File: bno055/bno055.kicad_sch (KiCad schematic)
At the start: 0 parts

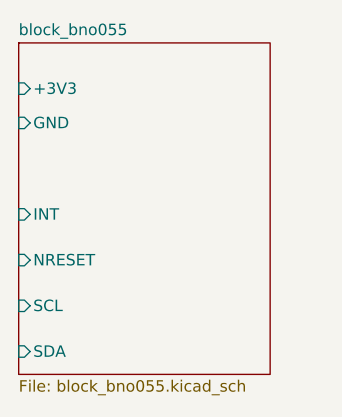
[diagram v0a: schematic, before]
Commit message: [Rushil] corrected pcb added information on both schematic and pcb user drawing correct circuit of bno055
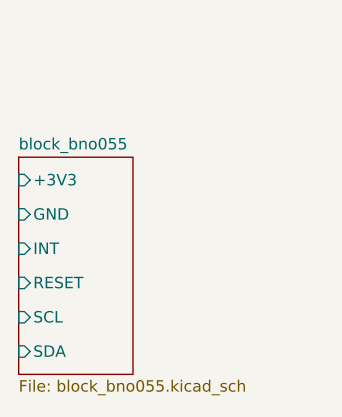
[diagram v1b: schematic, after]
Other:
- sheet block_bno055 ports: added RESET; removed NRESET
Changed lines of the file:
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@@
 	(paper "A4")
 	(sheet
-		(at 109.22 68.58)
-		(size 27.94 36.83)
+		(at 109.22 81.28)
+		(size 12.7 24.13)
 		(exclude_from_sim no)
 		(in_bom yes)
@@
 		)
 		(property "Sheetname" "block_bno055"
-			(at 109.22 67.8684 0)
+			(at 109.22 80.5684 0)
 			(effects
 				(font
@@
 		)
 		(pin "+3V3" input
-			(at 109.22 73.66 180)
+			(at 109.22 83.82 180)
 			(effects
 				(font
@@
 		)
 		(pin "GND" input
-			(at 109.22 77.47 180)
+			(at 109.22 87.63 180)
 			(effects
 				(font
@@
 		)
 		(pin "INT" input
-			(at 109.22 87.63 180)
-			(effects
-				(font
-					(size 1.27 1.27)
-				)
-				(justify left)
-			)
-		)
-		(pin "NRESET" input
-			(at 109.22 92.71 180)
+			(at 109.22 91.44 180)
 			(effects
 				(font
@@
 		)
 		(pin "SCL" input
-			(at 109.22 97.79 180)
+			(at 109.22 99.06 180)
 			(effects
 				(font
@@
 			(effects
 				(font
+					(size 1.27 1.27)
+				)
+				(justify left)
+			)
+		)
+		(pin "RESET" input
+			(at 109.22 95.25 180)
+			(effects
+				(font

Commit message: fixed BNO055
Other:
- sheet block_bno055 ports: added 3V3; removed +3V3
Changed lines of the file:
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@@
 			)
 		)
-		(pin "+3V3" input
+		(pin "3V3" input
 			(at 109.22 83.82 180)
 			(effects

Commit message: finalized BNO055
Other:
- sheet block_bno055 renamed BNO055
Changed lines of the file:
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@@
 			(color 0 0 0 0.0000)
 		)
-		(property "Sheetname" "block_bno055"
+		(property "Sheetname" "BNO055"
 			(at 109.22 80.5684 0)
 			(effects
